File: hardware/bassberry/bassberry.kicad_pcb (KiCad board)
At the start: 4 copper layers, 180 x 110 mm, 183 parts, among them J101 RPi 40-pin (face-down socket), J201 SAT LEFT, J202 SAT RIGHT, J203 SUB, J301 USB-C (charge + console), J401 3S BMS module (B-,B1,B2,B+,P-), J402 NTC 10k B3380 on cell, J501 SWIO (WCH-LinkE), J502 OLED 1.3in I2C (GND VCC SCL S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, Q301 40V N-MOS 5mR (AER4061BE equi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, Q302 40V N-MOS 5mR (AER4061BE equi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, Q303 40V N-MOS 5mR (AER4061BE equi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, Q304 40V N-MOS 5mR (AER4061BE equi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, Q305 30V N-MOS (RU3030M2) opt., SW301 PWRBANK (optional), SW501 POWER, SW502 BT, SW503 PLAY/PAUSE, SW504 VOL-, SW505 VOL+, SW506 EC11 encoder + push, U101 24C32 (HAT ID), U201 TAS5805M, U202 TAS5805M, U301 USBLC6-2SC6, U302 IP2366, U303 TPS565208, U304 MT3608, U305 HT7533-1, U306 HT7533-1, U501 CH32V003F4P6, U502 CH340C

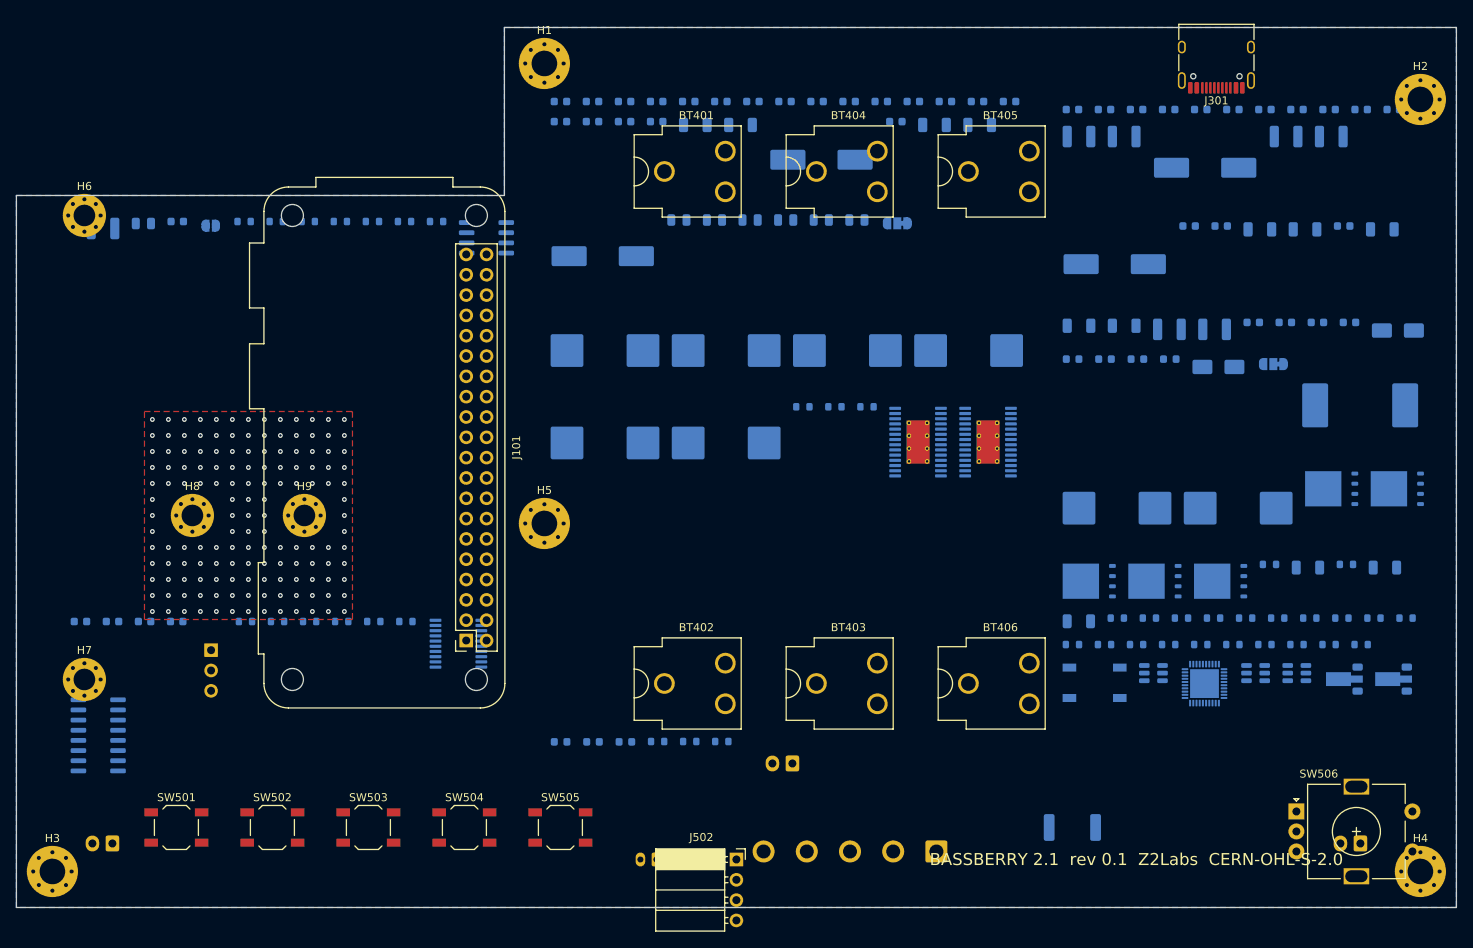
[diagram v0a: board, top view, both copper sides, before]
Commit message: rev 0.2 board: routed with srouter, DRC 0 errors / 0 unconnected / 0 parity, digital twin 1-4 PASS; KiCad files, reports, renders
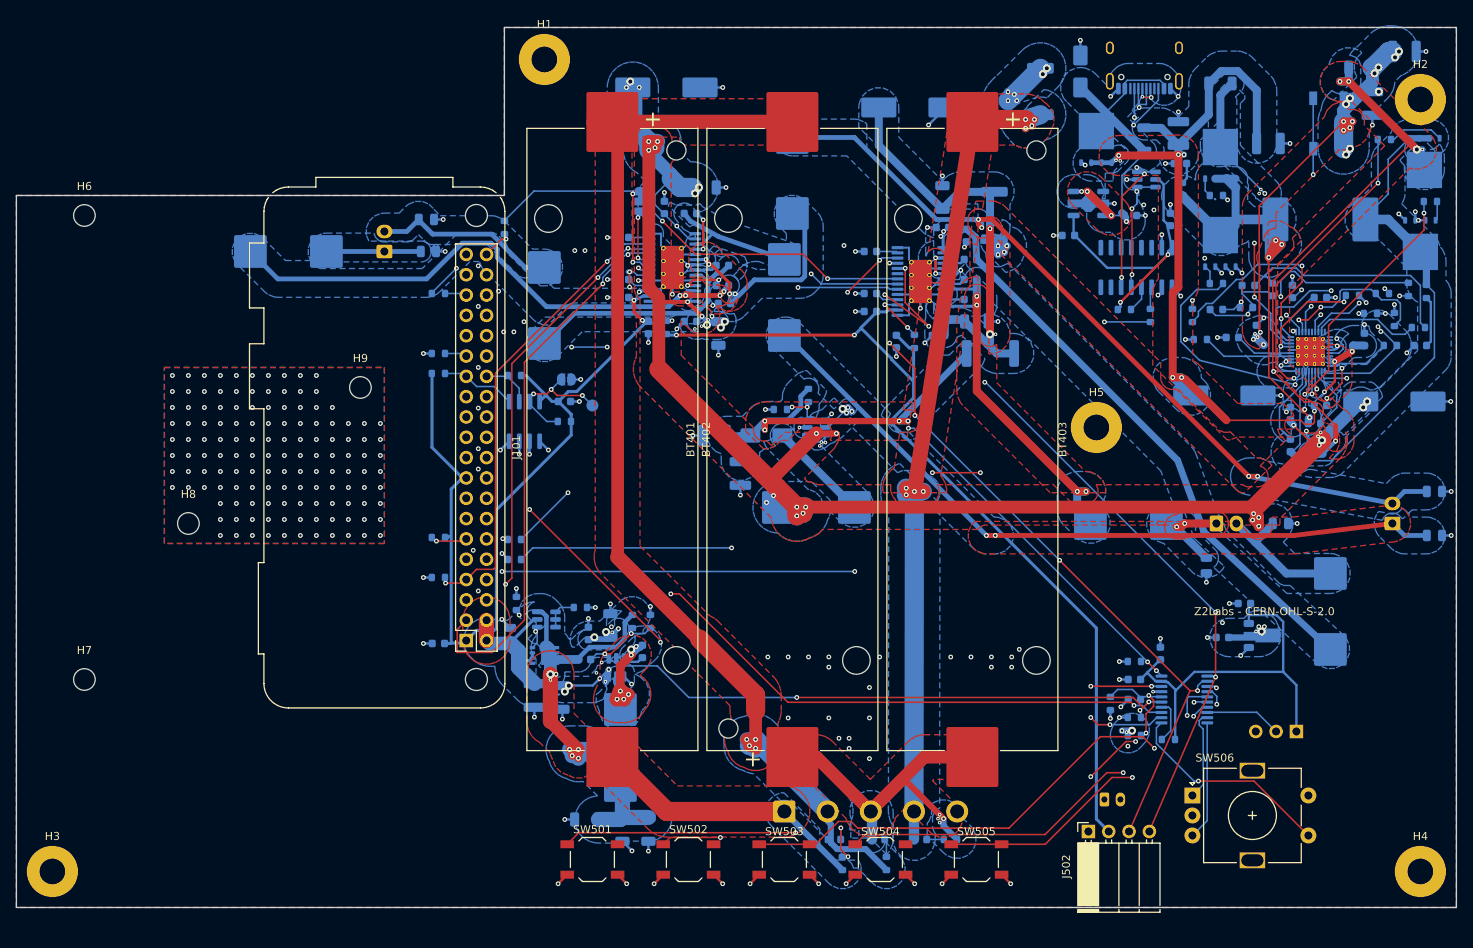
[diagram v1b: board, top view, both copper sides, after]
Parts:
- removed BT404: cell 2 -, BatteryClip_Keystone_54_D16-19mm
- removed BT405: cell 3 +, BatteryClip_Keystone_54_D16-19mm
- removed BT406: cell 3 -, BatteryClip_Keystone_54_D16-19mm
- removed JP301: PVDD_SUB select, SolderJumper-3_P1.3mm_Bridged12_RoundedPad1.0x1.5mm
- added C104: 100n, Capacitor_SMD:C_0603_1608Metric, B.Cu at (118.5, 96.8)
- added Q101: DMP3013SFV, Package_SON:Diodes_PowerDI3333-8, B.Cu at (116.0, 128.5)
- added Q102: DMMT5401, Package_TO_SOT_SMD:SOT-23-6, B.Cu at (116.2, 124.0)
- added R108: 10k 1%, Resistor_SMD:R_0603_1608Metric, B.Cu at (120.5, 122.5)
- added R109: 47k 1%, Resistor_SMD:R_0603_1608Metric, B.Cu at (112.5, 122.0)
- added R202: 10k, Resistor_SMD:R_0603_1608Metric, B.Cu at (102.8, 90.8)
- added R344: 0R 2512 (PVDD_SUB = battery), Resistor_SMD:R_2512_6332Metric, B.Cu at (172.2, 73.5)
- added R345: DNP 0R 2512 (PVDD_SUB = boost), Resistor_SMD:R_2512_6332Metric, B.Cu at (171.8, 90.8)
- added TP101: ID_WP, TestPoint:TestPoint_Pad_D1.5mm, B.Cu at (122.0, 97.2)
- BT401: value cell 1 + -> 18650 cell 1 (Keystone 1042); footprint BatteryClip_Keystone_54_D16-19mm -> Battery:BatteryHolder_Keystone_1042_1x18650
- BT402: value cell 1 - -> 18650 cell 2 (Keystone 1042); footprint BatteryClip_Keystone_54_D16-19mm -> Battery:BatteryHolder_Keystone_1042_1x18650
- BT403: value cell 2 + -> 18650 cell 3 (Keystone 1042); footprint BatteryClip_Keystone_54_D16-19mm -> Battery:BatteryHolder_Keystone_1042_1x18650
- C101, C312, C313, C315, C316, C340, C341: footprint C_1210_3225Metric -> Capacitor_SMD:C_1210_3225Metric
- C102, C260, C261, C262, C263, C264, C265: footprint C_0805_2012Metric -> Capacitor_SMD:C_0805_2012Metric
- C103, C211, C212, C213, C214, C215, C216, C217, C218, C219, C221, C222, C223, C224, C225, C226, C227, C228, C229, C231, C241, C301, C302, C303, C304, C305, C306, C307, C308, C309, C310, C311, C330, C331, C334, C350, C351, C352, C353, C501, C502, C503, C510: footprint C_0603_1608Metric -> Capacitor_SMD:C_0603_1608Metric
- C232, C233, C242, C243, C332, C333, C335, C336, C337: footprint C_1206_3216Metric -> Capacitor_SMD:C_1206_3216Metric
- C234, C244, C314, C317: footprint CP_Elec_10x10.5 -> Capacitor_SMD:CP_Elec_10x10.5
- D301, D306: footprint D_SMA -> Diode_SMD:D_SMA
- D302, D303, D304, D305, D401, D402, D403: footprint LED_0603_1608Metric -> LED_SMD:LED_0603_1608Metric
- F401: footprint Fuse_2512_6332Metric -> Fuse:Fuse_2512_6332Metric
- H1, H2, H3, H4, H5: value MountingHole_3.2mm_M3_Pad_Via -> MountingHole_3.2mm_M3_Pad; footprint MountingHole_3.2mm_M3_Pad_Via -> MountingHole:MountingHole_3.2mm_M3_Pad
- H6, H7, H8, H9: value MountingHole_2.7mm_M2.5_Pad_Via -> MountingHole_2.7mm_M2.5; footprint MountingHole_2.7mm_M2.5_Pad_Via -> MountingHole:MountingHole_2.7mm_M2.5
- J101: footprint Raspberry_Pi_Zero_Socketed_THT_FaceDown_MountingHoles -> Module:Raspberry_Pi_Zero_Socketed_THT_FaceDown_MountingHoles
- J201, J202, J203: footprint JST_XH_B2B-XH-A_1x02_P2.50mm_Vertical -> Connector_JST:JST_XH_B2B-XH-A_1x02_P2.50mm_Vertical
- J301: footprint USB_C_Receptacle_HRO_TYPE-C-31-M-12 -> Connector_USB:USB_C_Receptacle_HRO_TYPE-C-31-M-12; moved to B.Cu
- J401: footprint SolderWire-1sqmm_1x05_P5.4mm_D1.4mm_OD2.7mm -> Connector_Wire:SolderWire-1sqmm_1x05_P5.4mm_D1.4mm_OD2.7mm
- J402: footprint JST_PH_B2B-PH-K_1x02_P2.00mm_Vertical -> Connector_JST:JST_PH_B2B-PH-K_1x02_P2.00mm_Vertical
- J501: footprint PinHeader_1x03_P2.54mm_Vertical -> Connector_PinHeader_2.54mm:PinHeader_1x03_P2.54mm_Vertical
- J502: footprint PinSocket_1x04_P2.54mm_Horizontal -> Connector_PinSocket_2.54mm:PinSocket_1x04_P2.54mm_Horizontal
- JP101: footprint SolderJumper-2_P1.3mm_Open_RoundedPad1.0x1.5mm -> Jumper:SolderJumper-2_P1.3mm_Open_RoundedPad1.0x1.5mm
- JP201: footprint SolderJumper-3_P1.3mm_Bridged12_RoundedPad1.0x1.5mm -> Jumper:SolderJumper-3_P1.3mm_Bridged12_RoundedPad1.0x1.5mm
- L201, L202, L203, L204, L302, L303: footprint L_Changjiang_FXL1040 -> Inductor_SMD:L_Changjiang_FXL1040
- L205, L206: footprint L_Changjiang_FXL1050 -> Inductor_SMD:L_Changjiang_FXL1050
- L301: footprint L_Sunlord_MWSA1265S -> Inductor_SMD:L_Sunlord_MWSA1265S
- Q301, Q302, Q303, Q304, Q305: footprint TDSON-8-1 -> Package_TO_SOT_SMD:TDSON-8-1
- R101, R102, R103, R104, R105, R106, R201, R211, R221, R301, R303, R306, R307, R308, R309, R310, R311, R312, R313, R314, R315, R316, R317, R320, R321, R331, R332, R333, R341, R342, R343, R401, R402, R403, R501, R502, R503, R510, R511, R512: footprint R_0603_1608Metric -> Resistor_SMD:R_0603_1608Metric
- R107: value 10k -> 1k; footprint R_0603_1608Metric -> Resistor_SMD:R_0603_1608Metric
- R302, R304, R305: footprint R_1206_3216Metric -> Resistor_SMD:R_1206_3216Metric
- SW301, SW501, SW502, SW503, SW504, SW505: footprint SW_SPST_TL3342 -> Button_Switch_SMD:SW_SPST_TL3342
- SW506: footprint RotaryEncoder_Alps_EC11E-Switch_Vertical_H20mm -> Rotary_Encoder:RotaryEncoder_Alps_EC11E-Switch_Vertical_H20mm
- U101: value 24C32 (HAT ID) -> CAT24C32WI-GT3; footprint SOIC-8_3.9x4.9mm_P1.27mm -> Package_SO:SOIC-8_3.9x4.9mm_P1.27mm
- U201, U202: footprint HTSSOP-28-1EP_4.4x9.7mm_P0.65mm_EP2.85x5.4mm_ThermalVias -> Package_SO:HTSSOP-28-1EP_4.4x9.7mm_P0.65mm_EP2.85x5.4mm_ThermalVias
- U301, U303, U304: footprint SOT-23-6 -> Package_TO_SOT_SMD:SOT-23-6
- U302: footprint QFN-40-1EP_5x5mm_P0.4mm_EP3.6x3.6mm -> Package_DFN_QFN:QFN-40-1EP_5x5mm_P0.4mm_EP3.6x3.6mm_ThermalVias
- U305: footprint SOT-89-3 -> Package_TO_SOT_SMD:SOT-89-3
- U306: value HT7533-1 -> XC6216B332PR; footprint SOT-89-3 -> Package_TO_SOT_SMD:SOT-89-5
- U501: footprint TSSOP-20_4.4x6.5mm_P0.65mm -> Package_SO:TSSOP-20_4.4x6.5mm_P0.65mm
- U502: footprint SOIC-16_3.9x9.9mm_P1.27mm -> Package_SO:SOIC-16_3.9x9.9mm_P1.27mm
- moved U502 142.3 mm to (190.0, 80.0), turned to 90 degrees
- moved J501 136.0 mm to (210.0, 138.0), turned to 90 degrees
- moved C510 134.0 mm to (194.2, 74.0), turned to 90 degrees
- moved C501 131.9 mm to (189.8, 131.5)
- moved C502 131.0 mm to (193.0, 128.2), turned to 90 degrees
- moved C503 124.1 mm to (189.8, 134.0)
- moved C335 121.0 mm to (125.8, 150.2), turned to -90 degrees
- moved R501 116.3 mm to (194.0, 139.0)
- moved R502 108.0 mm to (189.8, 138.5), turned to 0 degrees
- moved C334 107.3 mm to (121.5, 125.8), turned to 90 degrees
- moved C332 105.0 mm to (118.2, 133.8), turned to -90 degrees
- moved R511 104.3 mm to (191.8, 86.0), turned to 90 degrees
- moved R503 100.6 mm to (186.8, 134.5), turned to -90 degrees
- moved C333 100.0 mm to (124.2, 124.8), turned to 90 degrees
- moved R512 97.9 mm to (188.5, 85.2)
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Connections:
- net /Audio: 2x TAS5805M (stereo BTL + sub PBTL)/AMP1_ADR renamed /audio/AMP1_ADR
- net /Audio: 2x TAS5805M (stereo BTL + sub PBTL)/AMP1_AN renamed /audio/AMP1_AN
- net /Audio: 2x TAS5805M (stereo BTL + sub PBTL)/AMP1_AP renamed /audio/AMP1_AP
- net /Audio: 2x TAS5805M (stereo BTL + sub PBTL)/AMP1_AVDD renamed /audio/AMP1_AVDD
- net /Audio: 2x TAS5805M (stereo BTL + sub PBTL)/AMP1_BN renamed /audio/AMP1_BN
- net /Audio: 2x TAS5805M (stereo BTL + sub PBTL)/AMP1_BP renamed /audio/AMP1_BP
- net /Audio: 2x TAS5805M (stereo BTL + sub PBTL)/AMP1_BSTAN renamed /audio/AMP1_BSTAN
- net /Audio: 2x TAS5805M (stereo BTL + sub PBTL)/AMP1_BSTAP renamed /audio/AMP1_BSTAP
- net /Audio: 2x TAS5805M (stereo BTL + sub PBTL)/AMP1_BSTBN renamed /audio/AMP1_BSTBN
- net /Audio: 2x TAS5805M (stereo BTL + sub PBTL)/AMP1_BSTBP renamed /audio/AMP1_BSTBP
- net /Audio: 2x TAS5805M (stereo BTL + sub PBTL)/AMP1_SDOUT renamed /audio/AMP1_SDOUT
- net /Audio: 2x TAS5805M (stereo BTL + sub PBTL)/AMP1_VRDIG renamed /audio/AMP1_VRDIG
- net /Audio: 2x TAS5805M (stereo BTL + sub PBTL)/AMP2_ADR renamed /audio/AMP2_ADR
- net /Audio: 2x TAS5805M (stereo BTL + sub PBTL)/AMP2_AVDD renamed /audio/AMP2_AVDD
- net /Audio: 2x TAS5805M (stereo BTL + sub PBTL)/AMP2_BSTAN renamed /audio/AMP2_BSTAN
- net /Audio: 2x TAS5805M (stereo BTL + sub PBTL)/AMP2_BSTAP renamed /audio/AMP2_BSTAP
- net /Audio: 2x TAS5805M (stereo BTL + sub PBTL)/AMP2_BSTBN renamed /audio/AMP2_BSTBN
- net /Audio: 2x TAS5805M (stereo BTL + sub PBTL)/AMP2_BSTBP renamed /audio/AMP2_BSTBP
- net /Audio: 2x TAS5805M (stereo BTL + sub PBTL)/AMP2_N renamed /audio/AMP2_N
- net /Audio: 2x TAS5805M (stereo BTL + sub PBTL)/AMP2_P renamed /audio/AMP2_P
- net /Audio: 2x TAS5805M (stereo BTL + sub PBTL)/AMP2_SDIN renamed /audio/AMP2_SDIN
- net /Audio: 2x TAS5805M (stereo BTL + sub PBTL)/AMP2_VRDIG renamed /audio/AMP2_VRDIG
- net /Audio: 2x TAS5805M (stereo BTL + sub PBTL)/SAT_L_N renamed /audio/SAT_L_N
- net /Audio: 2x TAS5805M (stereo BTL + sub PBTL)/SAT_L_P renamed /audio/SAT_L_P
- net /Audio: 2x TAS5805M (stereo BTL + sub PBTL)/SAT_R_N renamed /audio/SAT_R_N
- net /Audio: 2x TAS5805M (stereo BTL + sub PBTL)/SAT_R_P renamed /audio/SAT_R_P
- net /Audio: 2x TAS5805M (stereo BTL + sub PBTL)/SUB_N renamed /audio/SUB_N
- net /Audio: 2x TAS5805M (stereo BTL + sub PBTL)/SUB_P renamed /audio/SUB_P
- net /Battery: 3S 18650 clips, BMS module, protection/REV1 renamed /battery/REV1
- net /Battery: 3S 18650 clips, BMS module, protection/REV2 renamed /battery/REV2
- net /Battery: 3S 18650 clips, BMS module, protection/REV3 renamed /battery/REV3
- net /Power: USB-C PD charger (IP2366), 5V/5A Pi buck, sub boost, 3V3 LDOs/BOOST_FB renamed /power/BOOST_FB
- net /Power: USB-C PD charger (IP2366), 5V/5A Pi buck, sub boost, 3V3 LDOs/BOOST_OUT renamed /power/BOOST_OUT
- net /Power: USB-C PD charger (IP2366), 5V/5A Pi buck, sub boost, 3V3 LDOs/BOOST_SW renamed /power/BOOST_SW
- net /Power: USB-C PD charger (IP2366), 5V/5A Pi buck, sub boost, 3V3 LDOs/BUCK_BST renamed /power/BUCK_BST
- net /Power: USB-C PD charger (IP2366), 5V/5A Pi buck, sub boost, 3V3 LDOs/BUCK_FB renamed /power/BUCK_FB
- net /Power: USB-C PD charger (IP2366), 5V/5A Pi buck, sub boost, 3V3 LDOs/BUCK_SW renamed /power/BUCK_SW
- net /Power: USB-C PD charger (IP2366), 5V/5A Pi buck, sub boost, 3V3 LDOs/CC1 renamed /power/CC1
- net /Power: USB-C PD charger (IP2366), 5V/5A Pi buck, sub boost, 3V3 LDOs/CC2 renamed /power/CC2
- net /Power: USB-C PD charger (IP2366), 5V/5A Pi buck, sub boost, 3V3 LDOs/CHG_BATNUM renamed /power/CHG_BATNUM
- net /Power: USB-C PD charger (IP2366), 5V/5A Pi buck, sub boost, 3V3 LDOs/CHG_BST1 renamed /power/CHG_BST1
- net /Power: USB-C PD charger (IP2366), 5V/5A Pi buck, sub boost, 3V3 LDOs/CHG_BST2 renamed /power/CHG_BST2
- net /Power: USB-C PD charger (IP2366), 5V/5A Pi buck, sub boost, 3V3 LDOs/CHG_CCBDO renamed /power/CHG_CCBDO
- net /Power: USB-C PD charger (IP2366), 5V/5A Pi buck, sub boost, 3V3 LDOs/CHG_CSN1 renamed /power/CHG_CSN1
- net /Power: USB-C PD charger (IP2366), 5V/5A Pi buck, sub boost, 3V3 LDOs/CHG_CSN2 renamed /power/CHG_CSN2
- net /Power: USB-C PD charger (IP2366), 5V/5A Pi buck, sub boost, 3V3 LDOs/CHG_EN renamed /power/CHG_EN
- net /Power: USB-C PD charger (IP2366), 5V/5A Pi buck, sub boost, 3V3 LDOs/CHG_HG1 renamed /power/CHG_HG1
- net /Power: USB-C PD charger (IP2366), 5V/5A Pi buck, sub boost, 3V3 LDOs/CHG_HG1_R renamed /power/CHG_HG1_R
- net /Power: USB-C PD charger (IP2366), 5V/5A Pi buck, sub boost, 3V3 LDOs/CHG_HG2 renamed /power/CHG_HG2
- net /Power: USB-C PD charger (IP2366), 5V/5A Pi buck, sub boost, 3V3 LDOs/CHG_HG2_R renamed /power/CHG_HG2_R
- net /Power: USB-C PD charger (IP2366), 5V/5A Pi buck, sub boost, 3V3 LDOs/CHG_KEY renamed /power/CHG_KEY
- net /Power: USB-C PD charger (IP2366), 5V/5A Pi buck, sub boost, 3V3 LDOs/CHG_LED_A_R renamed /power/CHG_LED_A_R
- net /Power: USB-C PD charger (IP2366), 5V/5A Pi buck, sub boost, 3V3 LDOs/CHG_LED_B_R renamed /power/CHG_LED_B_R
- net /Power: USB-C PD charger (IP2366), 5V/5A Pi buck, sub boost, 3V3 LDOs/CHG_LG1 renamed /power/CHG_LG1
- net /Power: USB-C PD charger (IP2366), 5V/5A Pi buck, sub boost, 3V3 LDOs/CHG_LG1_R renamed /power/CHG_LG1_R
- net /Power: USB-C PD charger (IP2366), 5V/5A Pi buck, sub boost, 3V3 LDOs/CHG_LG2 renamed /power/CHG_LG2
- net /Power: USB-C PD charger (IP2366), 5V/5A Pi buck, sub boost, 3V3 LDOs/CHG_LG2_R renamed /power/CHG_LG2_R
- net /Power: USB-C PD charger (IP2366), 5V/5A Pi buck, sub boost, 3V3 LDOs/CHG_LX1 renamed /power/CHG_LX1
- net /Power: USB-C PD charger (IP2366), 5V/5A Pi buck, sub boost, 3V3 LDOs/CHG_LX2 renamed /power/CHG_LX2
- net /Power: USB-C PD charger (IP2366), 5V/5A Pi buck, sub boost, 3V3 LDOs/CHG_NODEB renamed /power/CHG_NODEB
- net /Power: USB-C PD charger (IP2366), 5V/5A Pi buck, sub boost, 3V3 LDOs/CHG_NODEC renamed /power/CHG_NODEC
- net /Power: USB-C PD charger (IP2366), 5V/5A Pi buck, sub boost, 3V3 LDOs/CHG_PSET renamed /power/CHG_PSET
- net /Power: USB-C PD charger (IP2366), 5V/5A Pi buck, sub boost, 3V3 LDOs/CHG_SN1 renamed /power/CHG_SN1
- net /Power: USB-C PD charger (IP2366), 5V/5A Pi buck, sub boost, 3V3 LDOs/CHG_SN2 renamed /power/CHG_SN2
- net /Power: USB-C PD charger (IP2366), 5V/5A Pi buck, sub boost, 3V3 LDOs/CHG_VBUSG renamed /power/CHG_VBUSG
- net /Power: USB-C PD charger (IP2366), 5V/5A Pi buck, sub boost, 3V3 LDOs/CHG_VCC5V renamed /power/CHG_VCC5V
- net /Power: USB-C PD charger (IP2366), 5V/5A Pi buck, sub boost, 3V3 LDOs/CHG_VCCIO renamed /power/CHG_VCCIO
- net /Power: USB-C PD charger (IP2366), 5V/5A Pi buck, sub boost, 3V3 LDOs/CHG_VIN renamed /power/CHG_VIN
- net /Power: USB-C PD charger (IP2366), 5V/5A Pi buck, sub boost, 3V3 LDOs/CHG_VSET renamed /power/CHG_VSET
- net /Raspberry Pi (mounted face-down) + HAT ID/ID_SC renamed /pi/ID_SC
- net /Raspberry Pi (mounted face-down) + HAT ID/ID_SD renamed /pi/ID_SD
- net /Raspberry Pi (mounted face-down) + HAT ID/ID_WP renamed /pi/ID_WP
- net /Raspberry Pi (mounted face-down) + HAT ID/PI_BCLK renamed /pi/PI_BCLK
- net /Raspberry Pi (mounted face-down) + HAT ID/PI_DOUT renamed /pi/PI_DOUT
- net /Raspberry Pi (mounted face-down) + HAT ID/PI_LRCLK renamed /pi/PI_LRCLK
- net /UI + supervisor MCU (CH32V003), OLED, buttons, encoder, USB console/BTN_BT renamed /ui/BTN_BT
- net /UI + supervisor MCU (CH32V003), OLED, buttons, encoder, USB console/BTN_PLAY renamed /ui/BTN_PLAY
- net /UI + supervisor MCU (CH32V003), OLED, buttons, encoder, USB console/BTN_PWR renamed /ui/BTN_PWR
- net /UI + supervisor MCU (CH32V003), OLED, buttons, encoder, USB console/BTN_VOLDN renamed /ui/BTN_VOLDN
- net /UI + supervisor MCU (CH32V003), OLED, buttons, encoder, USB console/BTN_VOLUP renamed /ui/BTN_VOLUP
- net /UI + supervisor MCU (CH32V003), OLED, buttons, encoder, USB console/CH340_V3 renamed /ui/CH340_V3
- net /UI + supervisor MCU (CH32V003), OLED, buttons, encoder, USB console/CON_RXD renamed /ui/CON_RXD
- net /UI + supervisor MCU (CH32V003), OLED, buttons, encoder, USB console/CON_TXD renamed /ui/CON_TXD
- net /UI + supervisor MCU (CH32V003), OLED, buttons, encoder, USB console/ENC_A renamed /ui/ENC_A
- net /UI + supervisor MCU (CH32V003), OLED, buttons, encoder, USB console/ENC_B renamed /ui/ENC_B
- net /UI + supervisor MCU (CH32V003), OLED, buttons, encoder, USB console/ENC_SW renamed /ui/ENC_SW
- net /UI + supervisor MCU (CH32V003), OLED, buttons, encoder, USB console/MCU_NRST renamed /ui/MCU_NRST
- net /UI + supervisor MCU (CH32V003), OLED, buttons, encoder, USB console/SWIO renamed /ui/SWIO
- net /UI + supervisor MCU (CH32V003), OLED, buttons, encoder, USB console/VBAT_SENSE renamed /ui/VBAT_SENSE
- BT401 pad 1: /Battery: 3S 18650 clips, BMS module, protection/CELL1 -> /battery/CELL1
- BT402 pad 1: /Battery: 3S 18650 clips, BMS module, protection/CELL0 -> /battery/CELL2
- BT403 pad 1: /Battery: 3S 18650 clips, BMS module, protection/CELL2 -> /battery/CELL3
- C331 pad 1: +5V -> +5V_BUCK
- C335 pad 1: +5V -> +5V_BUCK
- C336 pad 1: +5V -> +5V_BUCK
- C337 pad 1: +5V -> +5V_BUCK
- D401 pad 1: /Battery: 3S 18650 clips, BMS module, protection/CELL1 -> /battery/CELL1
- D402 pad 1: /Battery: 3S 18650 clips, BMS module, protection/CELL2 -> /battery/CELL2
- D403 pad 1: /Battery: 3S 18650 clips, BMS module, protection/CELL3 -> /battery/CELL3
- F401 pad 1: /Battery: 3S 18650 clips, BMS module, protection/CELL3 -> /battery/CELL3
- J101 pad 29: unconnected-(J101-GPCLK1/GPIO05-Pad29) -> AMP2_PDN
- J401 pad 1: /Battery: 3S 18650 clips, BMS module, protection/CELL0 -> /battery/CELL0
- J401 pad 2: /Battery: 3S 18650 clips, BMS module, protection/CELL1 -> /battery/CELL1
- J401 pad 3: /Battery: 3S 18650 clips, BMS module, protection/CELL2 -> /battery/CELL2
- J401 pad 4: /Battery: 3S 18650 clips, BMS module, protection/CELL3 -> /battery/CELL3
- L302 pad 2: +5V -> +5V_BUCK
- R201 pad 1: +3V3 -> AMP_PDN
- R201 pad 2: AMP_PDN -> GND
- R331 pad 1: +5V -> +5V_BUCK
- R401 pad 2: /Battery: 3S 18650 clips, BMS module, protection/CELL0 -> /battery/CELL0
- R402 pad 2: /Battery: 3S 18650 clips, BMS module, protection/CELL1 -> /battery/CELL1
- R403 pad 2: /Battery: 3S 18650 clips, BMS module, protection/CELL2 -> /battery/CELL2
- U202 pad 12: AMP_PDN -> AMP2_PDN
- U306 pad 1: GND -> +3V3_USB
- U306 pad 2: VBUS -> GND
- U306 pad 3: +3V3_USB -> VBUS
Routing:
- net +BATT: track 0.00 -> 434.9 mm, vias 0 -> 95
- net +3V3: track 0.00 -> 224.2 mm, vias 0 -> 4
- net I2C_SDA: track 0.00 -> 201.3 mm, vias 0 -> 8
- net I2C_SCL: track 0.00 -> 192.5 mm, vias 0 -> 8
- net GND: track 0.00 -> 165.5 mm, vias 145 -> 279
- net /battery/CELL1: track 0.00 -> 137.3 mm, vias 0 -> 4
- net /power/CHG_VIN: track 0.00 -> 110.6 mm, vias 0 -> 11
- net /battery/CELL3: track 0.00 -> 110.0 mm, vias 0 -> 8
- net PI_IRQ: track 0.00 -> 105.6 mm, vias 0 -> 3
- net /audio/SAT_R_N: track 0.00 -> 102.4 mm, vias 0 -> 4
- net PI_SHUTDOWN_REQ: track 0.00 -> 99.0 mm, vias 0 -> 2
- net PI_POWEROFF: track 0.00 -> 96.7 mm, vias 0 -> 4
- net PI_TXD: track 0.00 -> 96.3 mm, vias 0 -> 3
- net /ui/CON_TXD: track 0.00 -> 94.5 mm, vias 0 -> 4
- net /audio/SAT_R_P: track 0.00 -> 93.6 mm, vias 0 -> 2
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- added copper zone on B.Cu, net +5V
- added copper zone on F.Cu, net +5V
- added copper zone on B.Cu, net +5V_BUCK
- added copper zone on F.Cu, net +5V_BUCK
- added copper zone on B.Cu, net +BATT
- added copper zone on F.Cu, net +BATT
- added copper zone on In1.Cu, net +BATT
- added copper zone on B.Cu, net /audio/AMP1_AN
- added copper zone on B.Cu, net /audio/AMP1_AP
- added copper zone on F.Cu, net /audio/AMP1_AP
- added copper zone on B.Cu, net /audio/AMP1_BN
- added copper zone on F.Cu, net /audio/AMP1_BN
- added copper zone on B.Cu, net /audio/AMP1_BP
- added copper zone on B.Cu, net /audio/AMP2_N
- added copper zone on B.Cu, net /audio/AMP2_P
- added copper zone on F.Cu, net /audio/AMP2_P
- added copper zone on B.Cu, net /audio/SAT_L_N
- added copper zone on B.Cu, net /audio/SAT_L_P
- added copper zone on B.Cu, net /audio/SAT_R_N
- added copper zone on F.Cu, net /audio/SAT_R_N
- added copper zone on B.Cu, net /audio/SAT_R_P
- added copper zone on F.Cu, net /audio/SAT_R_P
- added copper zone on B.Cu, net /audio/SUB_N
- added copper zone on B.Cu, net /audio/SUB_P
- added copper zone on F.Cu, net /audio/SUB_P
- added copper zone on B.Cu, net /battery/CELL0
- added copper zone on F.Cu, net /battery/CELL0
- added copper zone on In1.Cu, net /battery/CELL0
- added copper zone on B.Cu, net /battery/CELL1
- added copper zone on F.Cu, net /battery/CELL1
- added copper zone on In1.Cu, net /battery/CELL1
- added copper zone on B.Cu, net /battery/CELL2
- added copper zone on F.Cu, net /battery/CELL2
- added copper zone on In1.Cu, net /battery/CELL2
- added copper zone on B.Cu, net /battery/CELL3
- added copper zone on F.Cu, net /battery/CELL3
- added copper zone on In1.Cu, net /battery/CELL3
- added copper zone on B.Cu, net /power/BOOST_OUT
- added copper zone on F.Cu, net /power/BOOST_OUT
- added copper zone on B.Cu, net /power/BOOST_SW
- added copper zone on B.Cu, net /power/BUCK_SW
- added copper zone on F.Cu, net /power/BUCK_SW
- added copper zone on B.Cu, net /power/CHG_LX1
- added copper zone on F.Cu, net /power/CHG_LX1
- added copper zone on In1.Cu, net /power/CHG_LX1
- added copper zone on B.Cu, net /power/CHG_LX2
- added copper zone on B.Cu, net /power/CHG_NODEB
- added copper zone on In1.Cu, net /power/CHG_NODEB
- added copper zone on B.Cu, net /power/CHG_NODEC
- added copper zone on F.Cu, net /power/CHG_NODEC
- added copper zone on B.Cu, net /power/CHG_VIN
- added copper zone on F.Cu, net /power/CHG_VIN
- added copper zone on B.Cu, net PVDD_SUB
- added copper zone on F.Cu, net PVDD_SUB
- added copper zone on In1.Cu, net PVDD_SUB
- added copper zone on B.Cu, net VBUS
- added copper zone on F.Cu, net VBUS
- added copper zone on In1.Cu, net VBUS
- removed copper zone on In1.Cu, net GND
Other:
- board text added: "BASSBERRY 2.1 rev 0.2"
- board text added: "Z2Labs - CERN-OHL-S-2.0"
- board text removed: "BASSBERRY 2.1 rev 0.1 Z2Labs CERN-OHL-S-2.0"
